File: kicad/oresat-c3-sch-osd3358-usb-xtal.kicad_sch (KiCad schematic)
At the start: 43 parts, among them U1 OSD3358-512M-BSM, U11 RCLAMP0504FB, Y1 24MHz, Y2 Crystal

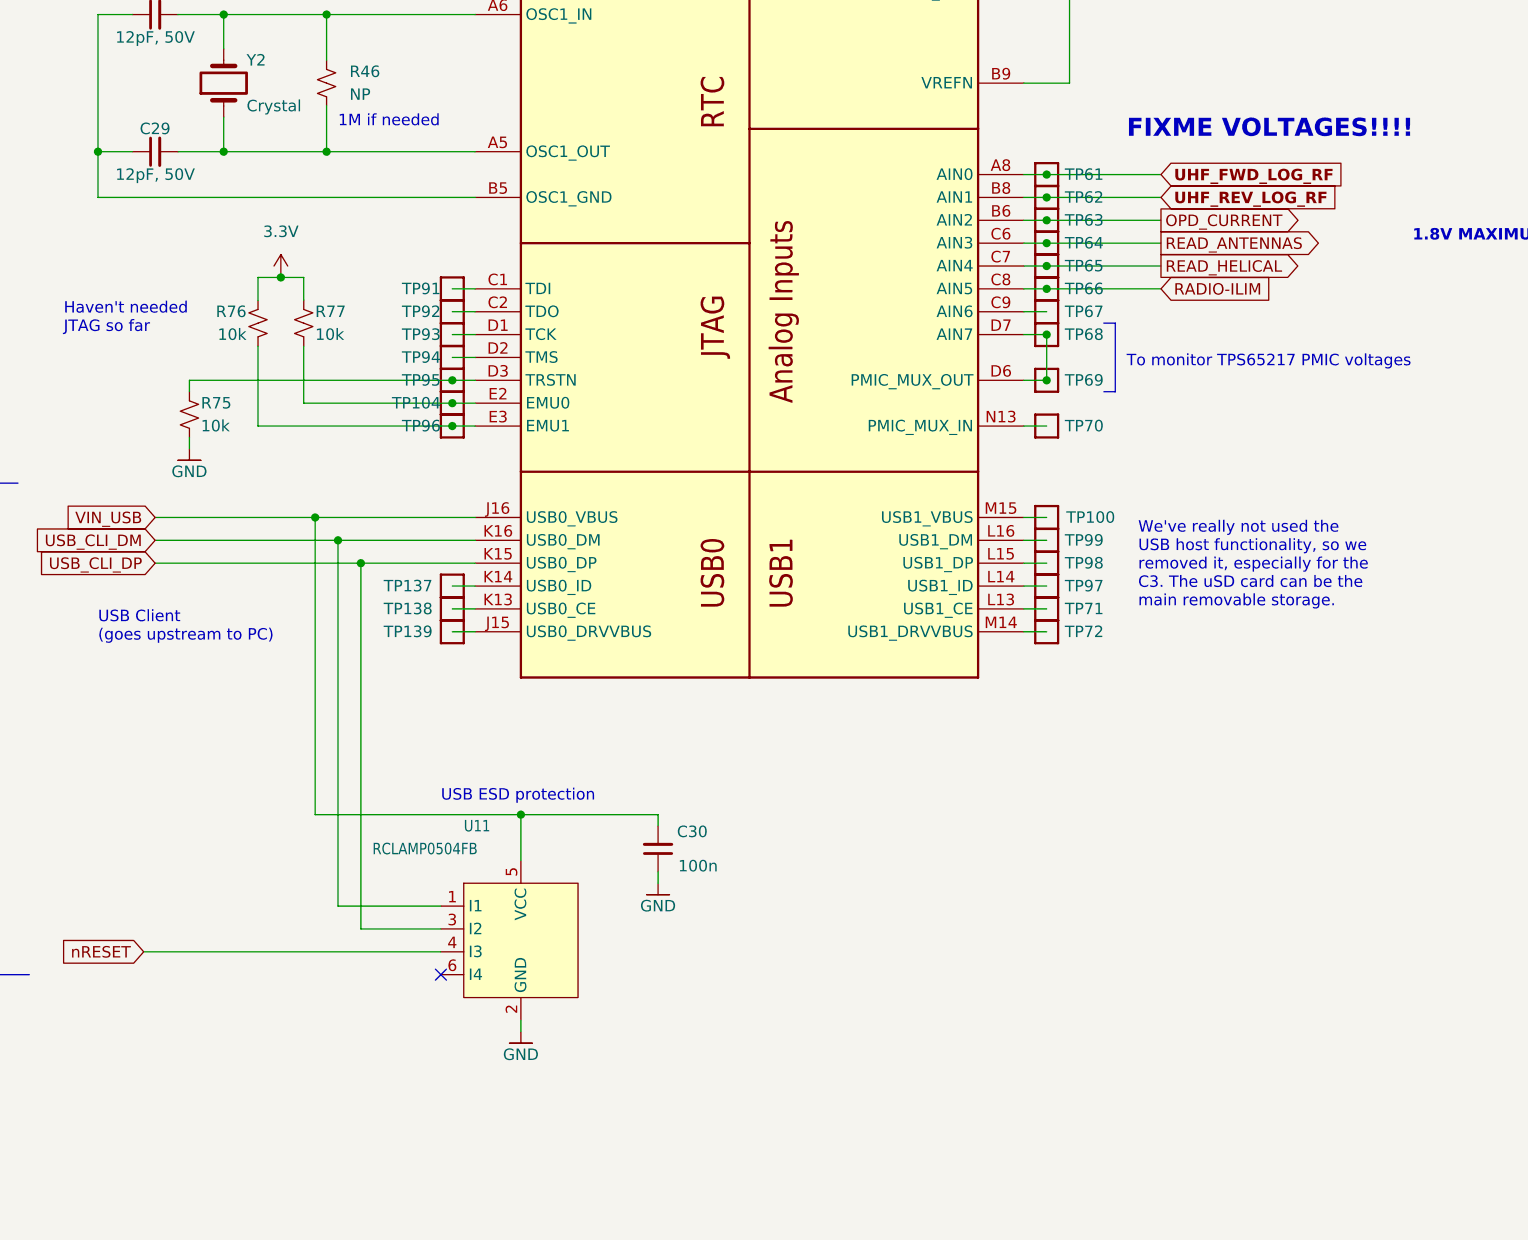
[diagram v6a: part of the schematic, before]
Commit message: Fixed footprints and laid out WDT and OPD circuitry.
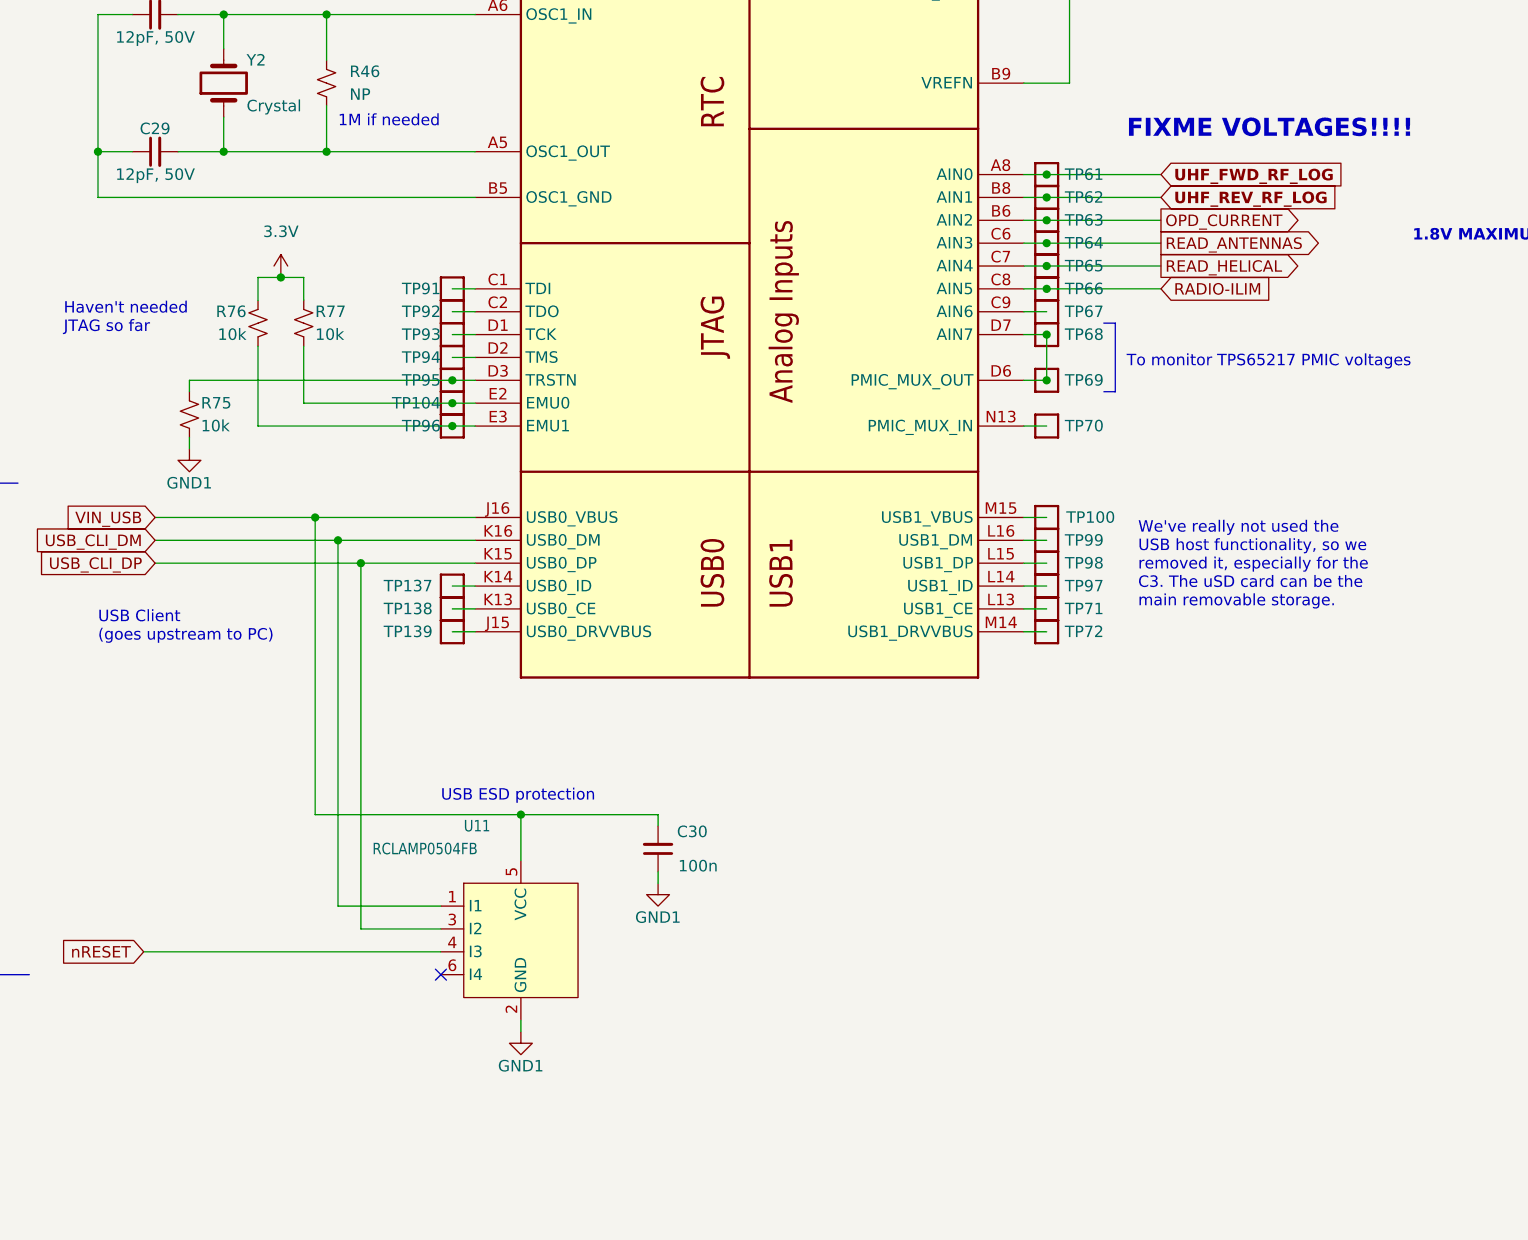
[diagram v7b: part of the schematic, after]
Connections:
- net GND renamed GND1
- net UHF_FWD_LOG_RF renamed UHF_FWD_RF_LOG
- net UHF_REV_LOG_RF renamed UHF_REV_RF_LOG
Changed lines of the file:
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@@
     )
   )
-  (global_label "UHF_FWD_LOG_RF" (shape input) (at 271.78 121.92 0) (fields_autoplaced)
+  (global_label "UHF_FWD_RF_LOG" (shape input) (at 271.78 121.92 0) (fields_autoplaced)
     (effects (font (size 1.27 1.27) (thickness 0.254) bold) (justify left))
     (property "Intersheetrefs" "${INTERSHEET_REFS}" (at 291.5638 121.92 0)
@@
     )
   )
-  (global_label "UHF_REV_LOG_RF" (shape input) (at 271.78 124.46 0) (fields_autoplaced)
+  (global_label "UHF_REV_RF_LOG" (shape input) (at 271.78 124.46 0) (fields_autoplaced)
     (effects (font (size 1.27 1.27) (thickness 0.254) bold) (justify left))
     (property "Intersheetrefs" "${INTERSHEET_REFS}" (at 291.2614 124.46 0)
@@
     )
   )
-  (symbol (lib_id "oresat-power:GND") (at 200.66 217.17 0) (unit 1)
-    (in_bom yes) (on_board yes) (dnp no)
-    (property "Reference" "#GND0163" (at 200.66 223.52 0)
-      (effects (font (size 1.27 1.27)) hide)
-    )
-    (property "Value" "GND" (at 200.66 219.71 0)
+  (symbol (lib_id "power:GND1") (at 200.66 217.17 0) (unit 1)
+    (in_bom yes) (on_board yes) (dnp no)
+    (property "Reference" "#PWR0147" (at 200.66 223.52 0)
+      (effects (font (size 1.27 1.27)) hide)
+    )
+    (property "Value" "GND1" (at 200.66 220.98 0)
       (effects (font (size 1.27 1.27)))
     )
@@
       (project "oresat-c3"
         (path "/65d12cdd-c326-4033-9053-c59fa4e0b25e/0d3a1fa4-c9ee-4335-9068-a81ae0178f3f"
-          (reference "#GND0163") (unit 1)
+          (reference "#PWR0147") (unit 1)
         )
       )
@@
     )
   )
-  (symbol (lib_id "oresat-power:GND") (at 163.83 152.4 0) (unit 1)
-    (in_bom yes) (on_board yes) (dnp no)
-    (property "Reference" "#GND0155" (at 163.83 158.75 0)
-      (effects (font (size 1.27 1.27)) hide)
-    )
-    (property "Value" "GND" (at 163.83 154.94 0)
+  (symbol (lib_id "power:GND1") (at 163.83 152.4 0) (unit 1)
+    (in_bom yes) (on_board yes) (dnp no)
+    (property "Reference" "#PWR0145" (at 163.83 158.75 0)
+      (effects (font (size 1.27 1.27)) hide)
+    )
+    (property "Value" "GND1" (at 163.83 156.21 0)
       (effects (font (size 1.27 1.27)))
     )
@@
       (project "oresat-c3"
         (path "/65d12cdd-c326-4033-9053-c59fa4e0b25e/0d3a1fa4-c9ee-4335-9068-a81ae0178f3f"
-          (reference "#GND0155") (unit 1)
+          (reference "#PWR0145") (unit 1)
         )
       )
@@
     )
   )
-  (symbol (lib_id "oresat-power:GND") (at 215.9 200.66 0) (unit 1)
-    (in_bom yes) (on_board yes) (dnp no)
-    (property "Reference" "#GND0164" (at 215.9 207.01 0)
-      (effects (font (size 1.27 1.27)) hide)
-    )
-    (property "Value" "GND" (at 215.9 203.2 0)
+  (symbol (lib_id "power:GND1") (at 215.9 200.66 0) (unit 1)
+    (in_bom yes) (on_board yes) (dnp no)
+    (property "Reference" "#PWR0146" (at 215.9 207.01 0)
+      (effects (font (size 1.27 1.27)) hide)
+    )
+    (property "Value" "GND1" (at 215.9 204.47 0)
       (effects (font (size 1.27 1.27)))
     )
@@
       (project "oresat-c3"
         (path "/65d12cdd-c326-4033-9053-c59fa4e0b25e/0d3a1fa4-c9ee-4335-9068-a81ae0178f3f"
-          (reference "#GND0164") (unit 1)
-        )
-      )
+          (reference "#PWR0146") (unit 1)
+        )
+      )

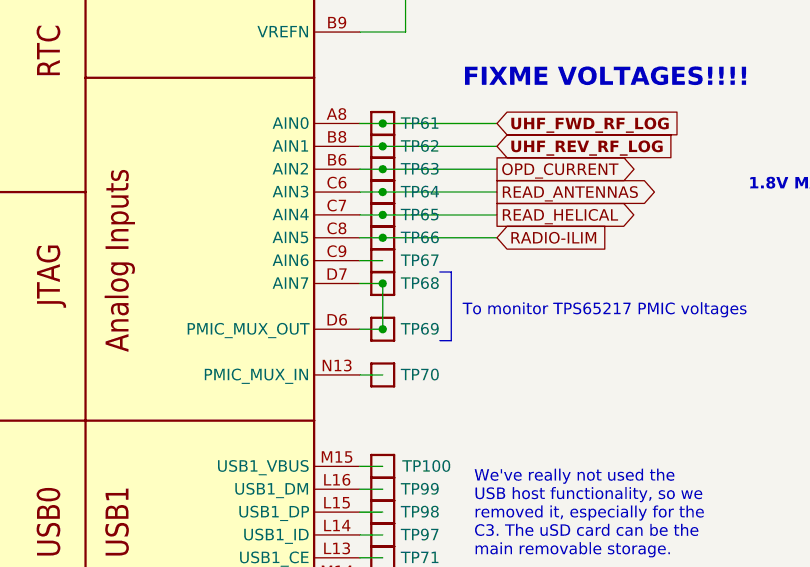
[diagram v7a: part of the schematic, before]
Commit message: routed everything but some minor lines and the radios. About to move the octavo and EVERYTHING else, wish me luck. Should give enough room for the radios!
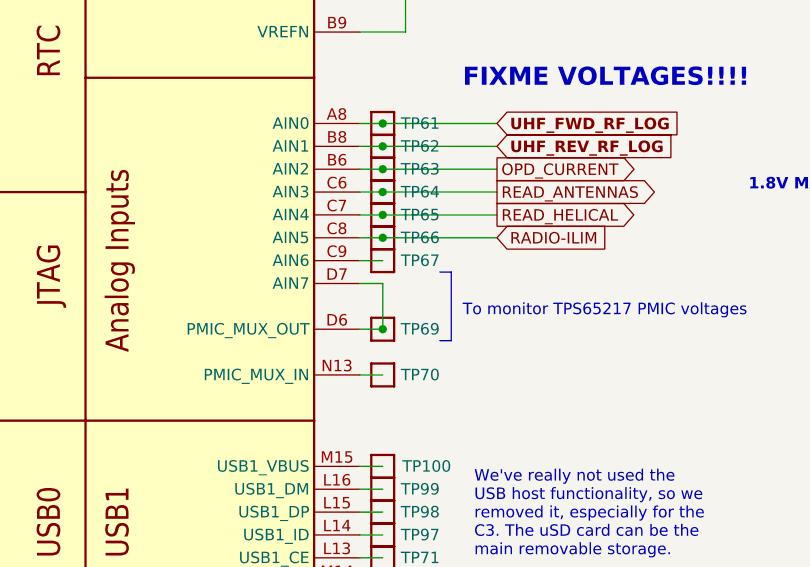
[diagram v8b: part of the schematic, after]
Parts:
- removed TP68: Test-Point, oresat-misc:TestPoint_Pad_D1.0mm, symbol oresat-misc:Test-Point-1mm-round
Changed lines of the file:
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@@
   (junction (at 147.32 88.9) (diameter 0) (color 0 0 0 0)
-  )
-  (junction (at 259.08 139.7) (diameter 0) (color 0 0 0 0)
   )
   (junction (at 167.64 119.38) (diameter 0) (color 0 0 0 0)
@@
         )
       )
-    )
-  )
-  (symbol (lib_id "oresat-misc:Test-Point-1mm-round") (at 259.08 139.7 180) (unit 1)
-    (in_bom yes) (on_board yes) (dnp no)
-    (property "Reference" "TP68" (at 265.43 139.7 0)
-      (effects (font (size 1.27 1.27)) (justify left))
-    )
-    (property "Value" "Test-Point" (at 259.08 142.24 0)
-      (effects (font (size 1.27 1.27)) hide)
-    )
-    (property "Footprint" "oresat-misc:TestPoint_Pad_D1.0mm" (at 259.08 149.86 0)
-      (effects (font (size 1.27 1.27)) hide)
-    )
-    (property "Datasheet" "" (at 259.08 139.7 0)
-      (effects (font (size 1.27 1.27)) hide)
-    )
-    (pin "1")
-    (instances
-      (project "oresat-c3"
-        (path "/65d12cdd-c326-4033-9053-c59fa4e0b25e/0d3a1fa4-c9ee-4335-9068-a81ae0178f3f"
-          (reference "TP68") (unit 1)
-        )
-      )
